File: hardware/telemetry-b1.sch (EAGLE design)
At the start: 119 parts, among them IC1 COPERNICUSSMD, IC10 TPS70933, IC2 TPS70933, IC4 STM32L073CZT6, IC5 TPS62160, IC6 HX1, IC7 LMP7702, IC9 HIH9131, J1 I2C1, J10 TEMP_BAT, J11 DNP, J12 INSOL, J13 SMA_EDGE, J2 I2C2, J3 SMA_EDGE, J4 USD-SOCKET, J5 BAT, J6 SMA_EDGE, J7 SMA_EDGE, J8 TEMP_GPS, J9 TEMP_HOT, K1 ARE104H, K2 ARE104H, Q1 AO3400A, Q2 AO3400A, U1 LTC3105, U2 INA219, Y1 32768, Y2 8M

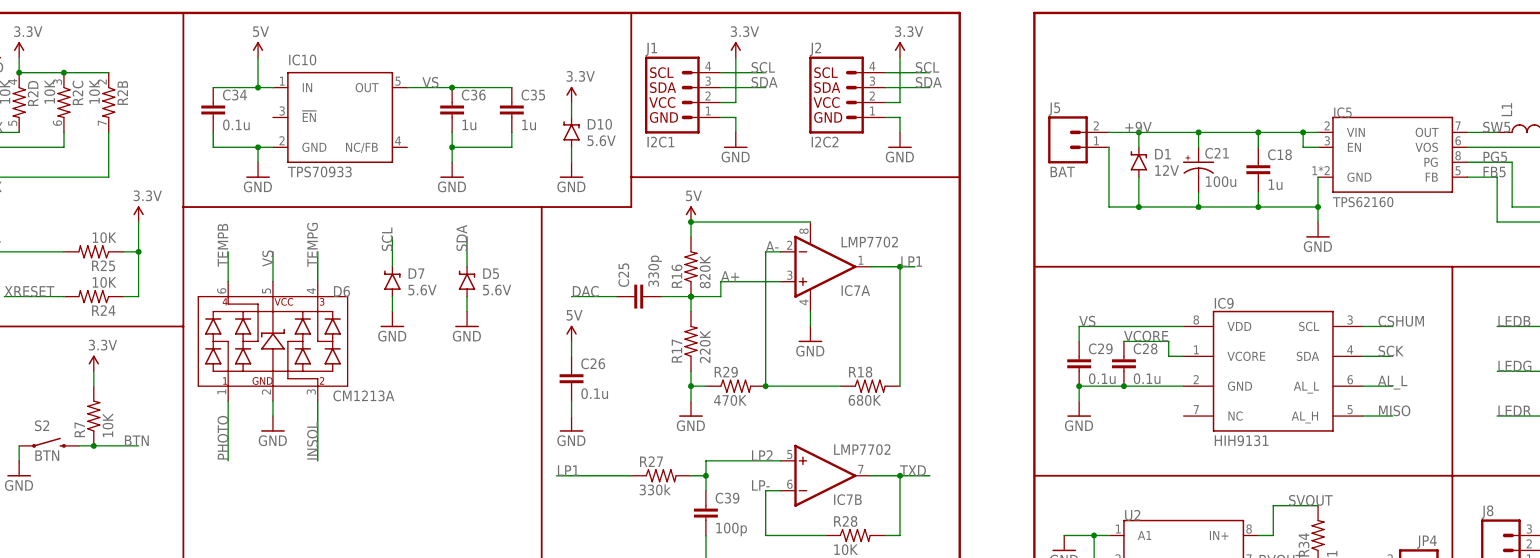
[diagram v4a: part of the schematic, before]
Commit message: Work on layout on beta PCB. Need to swap i2c and swd headers
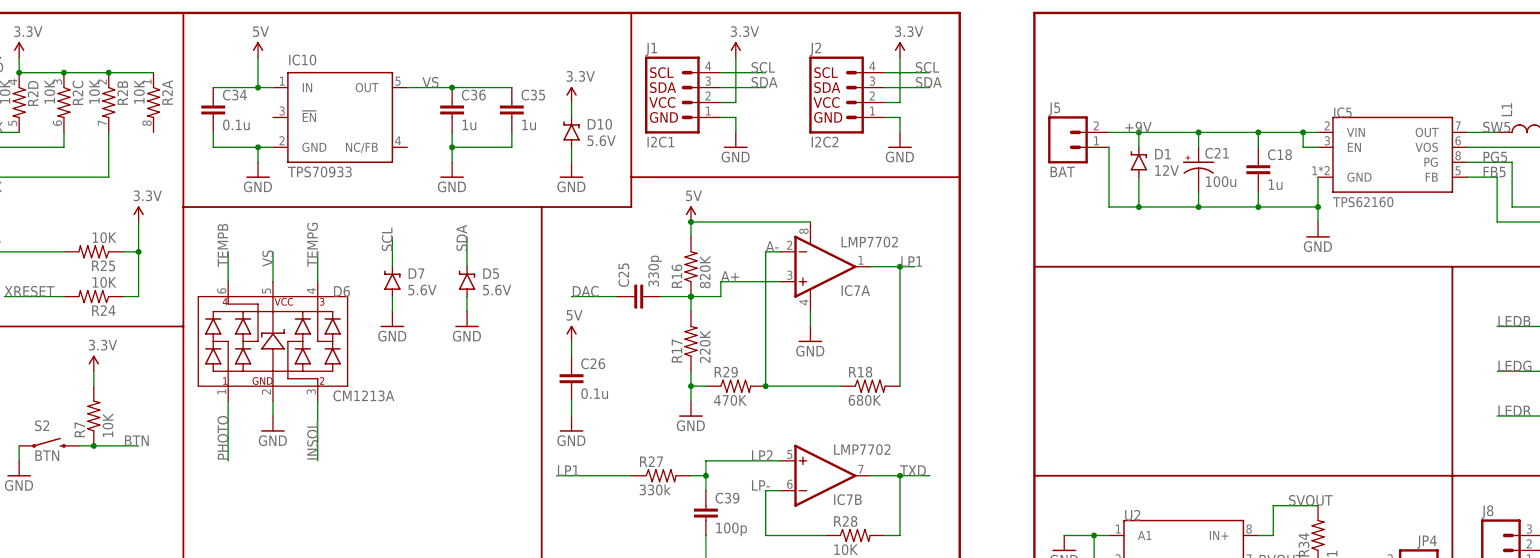
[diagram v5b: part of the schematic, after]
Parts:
- removed C28, C29: 0.1u, SparkFun-Passives:CAP0805
- removed IC9: HIH9131, SparkFun-AnalogIC:HIH6131
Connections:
- removed net AL_L: IC9.AL_L
- removed net VCORE: C28.1, IC9.VCORE
- net 3.3V: now also R2A.1
- net CSHUM: no longer IC9.SCL
- net GND: no longer C28.2, C29.2, IC9.GND
- net MISO: no longer IC9.AL_H
- net SCK: no longer IC9.SDA
- net VS: no longer C29.1, IC9.VDD
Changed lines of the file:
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@@
 <part name="SUPPLY24" library="SparkFun-Aesthetics" deviceset="3.3V" device=""/>
 <part name="C27" library="SparkFun-Passives" deviceset="CAP" device="0805" value="0.1u"/>
-<part name="IC9" library="SparkFun-AnalogIC" deviceset="HIH6131" device="" value="HIH9131"/>
-<part name="C28" library="SparkFun-Passives" deviceset="CAP" device="0805" value="0.1u"/>
-<part name="C29" library="SparkFun-Passives" deviceset="CAP" device="0805" value="0.1u"/>
-<part name="GND29" library="SparkFun-Aesthetics" deviceset="GND" device=""/>
 <part name="J6" library="SparkFun-Connectors" deviceset="SMA_EDGE" device=""/>
 <part name="J7" library="SparkFun-Connectors" deviceset="SMA_EDGE" device=""/>
@@
 <instance part="SUPPLY24" gate="G$1" x="220.98" y="76.2"/>
 <instance part="C27" gate="G$1" x="203.2" y="63.5"/>
-<instance part="IC9" gate="G$1" x="302.26" y="124.46"/>
-<instance part="C28" gate="G$1" x="276.86" y="124.46"/>
-<instance part="C29" gate="G$1" x="269.24" y="124.46"/>
-<instance part="GND29" gate="1" x="269.24" y="116.84"/>
 <instance part="J6" gate="1" x="474.98" y="170.18"/>
 <instance part="J7" gate="1" x="7.62" y="180.34"/>
@@
 <instance part="R34" gate="G$1" x="309.88" y="96.52" rot="R90"/>
 <instance part="JP4" gate="G$1" x="327.66" y="88.9" rot="MR0"/>
+<instance part="R2" gate="A" x="111.76" y="170.18" rot="R270"/>
 </instances>
 <busses>
@@
 <wire x1="203.2" y1="58.42" x2="203.2" y2="60.96" width="0.1524" layer="91"/>
 <junction x="220.98" y="58.42"/>
-</segment>
-<segment>
-<pinref part="GND29" gate="1" pin="GND"/>
-<pinref part="C29" gate="G$1" pin="2"/>
-<wire x1="269.24" y1="119.38" x2="269.24" y2="121.92" width="0.1524" layer="91"/>
-<pinref part="C28" gate="G$1" pin="2"/>
-<wire x1="269.24" y1="121.92" x2="276.86" y2="121.92" width="0.1524" layer="91"/>
-<junction x="269.24" y="121.92"/>
-<pinref part="IC9" gate="G$1" pin="GND"/>
-<wire x1="276.86" y1="121.92" x2="287.02" y2="121.92" width="0.1524" layer="91"/>
-<junction x="276.86" y="121.92"/>
 </segment>
 <segment>
@@
 <wire x1="96.52" y1="175.26" x2="104.14" y2="175.26" width="0.1524" layer="91"/>
 <junction x="96.52" y="175.26"/>
+<pinref part="R2" gate="A" pin="1"/>
+<wire x1="104.14" y1="175.26" x2="111.76" y2="175.26" width="0.1524" layer="91"/>
+<junction x="104.14" y="175.26"/>
 </segment>
 <segment>
@@
 <label x="213.36" y="60.96" size="1.778" layer="95"/>
 </segment>
-<segment>
-<pinref part="IC9" gate="G$1" pin="AL_H"/>
-<wire x1="322.58" y1="116.84" x2="317.5" y2="116.84" width="0.1524" layer="91"/>
-<label x="320.04" y="116.84" size="1.778" layer="95"/>
-</segment>
 </net>
 <net name="SCK" class="0">
@@
 <wire x1="213.36" y1="66.04" x2="223.52" y2="66.04" width="0.1524" layer="91"/>
 <label x="213.36" y="66.04" size="1.778" layer="95"/>
-</segment>
-<segment>
-<pinref part="IC9" gate="G$1" pin="SDA"/>
-<wire x1="322.58" y1="127" x2="317.5" y2="127" width="0.1524" layer="91"/>
-<label x="320.04" y="127" size="1.778" layer="95"/>
 </segment>
 </net>
@@
 </net>
 <net name="CSHUM" class="0">
-<segment>
-<pinref part="IC9" gate="G$1" pin="SCL"/>
-<wire x1="322.58" y1="132.08" x2="317.5" y2="132.08" width="0.1524" layer="91"/>
-<label x="320.04" y="132.08" size="1.778" layer="95"/>
-</segment>
 <segment>
 <pinref part="IC4" gate="G$1" pin="PB13"/>
@@
 </segment>
 </net>
-<net name="VCORE" class="0">
-<segment>
-<pinref part="IC9" gate="G$1" pin="VCORE"/>
-<wire x1="287.02" y1="127" x2="284.48" y2="127" width="0.1524" layer="91"/>
-<wire x1="284.48" y1="127" x2="284.48" y2="129.54" width="0.1524" layer="91"/>
-<pinref part="C28" gate="G$1" pin="1"/>
-<wire x1="284.48" y1="129.54" x2="276.86" y2="129.54" width="0.1524" layer="91"/>
-<label x="276.86" y="129.54" size="1.778" layer="95"/>
-</segment>
-</net>
 <net name="RF_GPS" class="0">
 <segment>
@@
 <wire x1="469.9" y1="109.22" x2="474.98" y2="109.22" width="0.1524" layer="91"/>
 <label x="472.44" y="109.22" size="1.778" layer="95"/>
-</segment>
-</net>
-<net name="AL_L" class="0">
-<segment>
-<pinref part="IC9" gate="G$1" pin="AL_L"/>
-<wire x1="322.58" y1="121.92" x2="317.5" y2="121.92" width="0.1524" layer="91"/>
-<label x="320.04" y="121.92" size="1.778" layer="95"/>
 </segment>
 </net>
@@
 </segment>
 <segment>
-<pinref part="IC9" gate="G$1" pin="VDD"/>
-<pinref part="C29" gate="G$1" pin="1"/>
-<wire x1="287.02" y1="132.08" x2="269.24" y2="132.08" width="0.1524" layer="91"/>
-<wire x1="269.24" y1="132.08" x2="269.24" y2="129.54" width="0.1524" layer="91"/>
-<label x="269.24" y="132.08" size="1.778" layer="95"/>
-</segment>
-<segment>

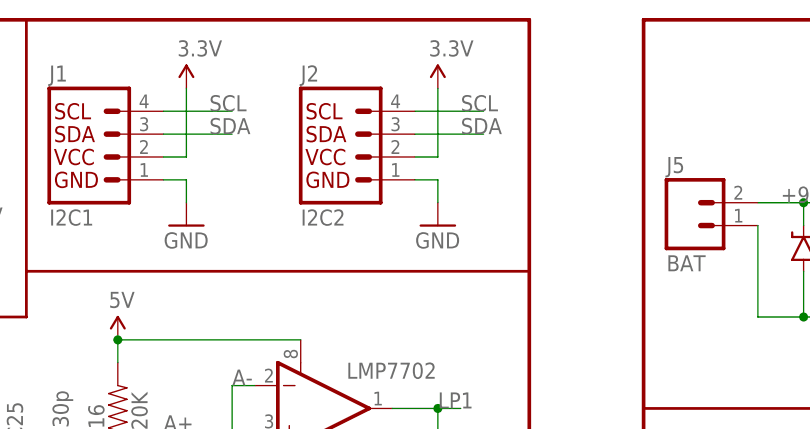
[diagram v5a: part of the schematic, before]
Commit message: Finish routing all traces on beta board. Needs a silkscreen pass.
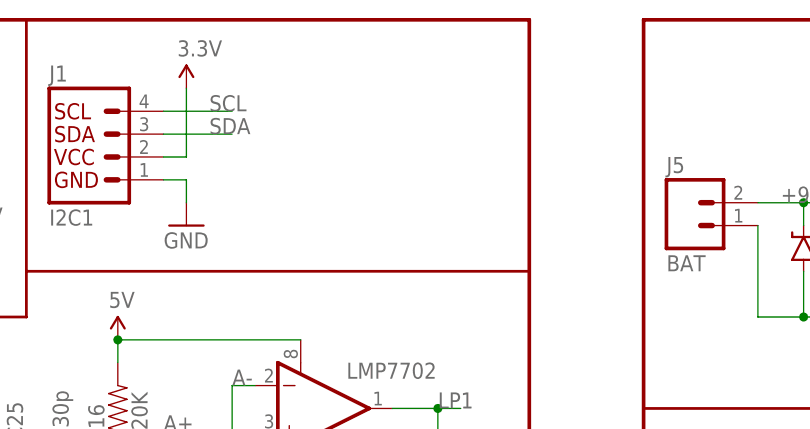
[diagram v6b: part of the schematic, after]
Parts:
- removed J2: I2C2, SparkFun-Connectors:I2C_STANDARD_NO_SILK
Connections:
- net 3.3V: no longer J2.2
- net GND: no longer J2.1
- net SCL: no longer J2.4
- net SDA: no longer J2.3
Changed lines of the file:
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@@
 <part name="SUPPLY12" library="SparkFun-Aesthetics" deviceset="3.3V" device=""/>
 <part name="J1" library="SparkFun-Connectors" deviceset="I2C_STANDARD" device="_NO_SILK" value="I2C1"/>
-<part name="J2" library="SparkFun-Connectors" deviceset="I2C_STANDARD" device="_NO_SILK" value="I2C2"/>
 <part name="SUPPLY13" library="SparkFun-Aesthetics" deviceset="3.3V" device=""/>
-<part name="SUPPLY14" library="SparkFun-Aesthetics" deviceset="3.3V" device=""/>
 <part name="GND17" library="SparkFun-Aesthetics" deviceset="GND" device=""/>
-<part name="GND18" library="SparkFun-Aesthetics" deviceset="GND" device=""/>
 <part name="R2" library="SparkFun-Passives" deviceset="RESISTOR-ARRAY" device="0603-ARV" value="10K"/>
 <part name="IC5" library="HAB" deviceset="TPS62160" device=""/>
@@
 <instance part="SUPPLY12" gate="G$1" x="101.6" y="124.46"/>
 <instance part="J1" gate="G$1" x="198.12" y="165.1"/>
-<instance part="J2" gate="G$1" x="226.06" y="165.1"/>
 <instance part="SUPPLY13" gate="G$1" x="210.82" y="177.8"/>
-<instance part="SUPPLY14" gate="G$1" x="238.76" y="177.8"/>
 <instance part="GND17" gate="1" x="210.82" y="162.56"/>
-<instance part="GND18" gate="1" x="238.76" y="162.56"/>
 <instance part="R2" gate="B" x="104.14" y="170.18" rot="R270"/>
 <instance part="R2" gate="C" x="96.52" y="170.18" rot="R270"/>
@@
 </segment>
 <segment>
-<pinref part="GND18" gate="1" pin="GND"/>
-<wire x1="238.76" y1="165.1" x2="238.76" y2="167.64" width="0.1524" layer="91"/>
-<pinref part="J2" gate="G$1" pin="1"/>
-<wire x1="238.76" y1="167.64" x2="236.22" y2="167.64" width="0.1524" layer="91"/>
-</segment>
-<segment>
 <pinref part="GND17" gate="1" pin="GND"/>
 <wire x1="210.82" y1="165.1" x2="210.82" y2="167.64" width="0.1524" layer="91"/>
@@
 </segment>
 <segment>
-<pinref part="SUPPLY14" gate="G$1" pin="3.3V"/>
-<wire x1="238.76" y1="177.8" x2="238.76" y2="170.18" width="0.1524" layer="91"/>
-<pinref part="J2" gate="G$1" pin="2"/>
-<wire x1="238.76" y1="170.18" x2="236.22" y2="170.18" width="0.1524" layer="91"/>
-</segment>
-<segment>
 <pinref part="J4" gate="G$1" pin="VCC"/>
 <wire x1="223.52" y1="68.58" x2="220.98" y2="68.58" width="0.1524" layer="91"/>
@@
 </segment>
 <segment>
-<pinref part="J2" gate="G$1" pin="4"/>
-<wire x1="243.84" y1="175.26" x2="236.22" y2="175.26" width="0.1524" layer="91"/>
-<label x="241.3" y="175.26" size="1.778" layer="95"/>
-</segment>
-<segment>
 <pinref part="D7" gate="G$1" pin="C"/>
 <wire x1="152.4" y1="142.24" x2="152.4" y2="147.32" width="0.1524" layer="91"/>
@@
 </segment>
 <segment>
-<pinref part="J2" gate="G$1" pin="3"/>
-<wire x1="243.84" y1="172.72" x2="236.22" y2="172.72" width="0.1524" layer="91"/>
-<label x="241.3" y="172.72" size="1.778" layer="95"/>
-</segment>
-<segment>

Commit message: Silkscreen gloss on beta board
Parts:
- J1: value I2C1 -> I2C
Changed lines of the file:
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@@
 <part name="GND16" library="SparkFun-Aesthetics" deviceset="GND" device=""/>
 <part name="SUPPLY12" library="SparkFun-Aesthetics" deviceset="3.3V" device=""/>
-<part name="J1" library="SparkFun-Connectors" deviceset="I2C_STANDARD" device="_NO_SILK" value="I2C1"/>
+<part name="J1" library="SparkFun-Connectors" deviceset="I2C_STANDARD" device="_NO_SILK" value="I2C"/>
 <part name="SUPPLY13" library="SparkFun-Aesthetics" deviceset="3.3V" device=""/>
 <part name="GND17" library="SparkFun-Aesthetics" deviceset="GND" device=""/>

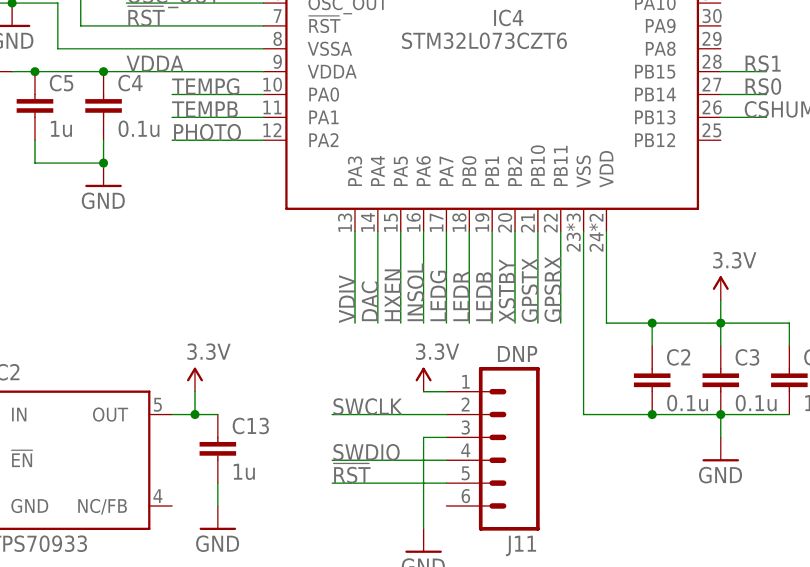
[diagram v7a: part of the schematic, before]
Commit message: Swap HXEN pin to 5VT pin
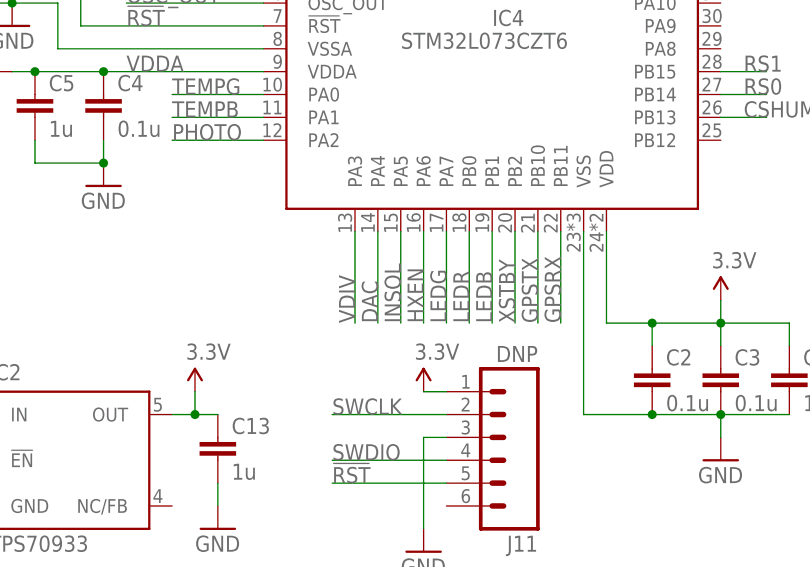
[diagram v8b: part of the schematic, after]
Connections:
- net HXEN: now also IC4.PA6; no longer IC4.PA5
- net INSOL: now also IC4.PA5; no longer IC4.PA6
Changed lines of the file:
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@@
 </segment>
 <segment>
-<pinref part="IC4" gate="G$1" pin="PA5"/>
-<wire x1="60.96" y1="30.48" x2="60.96" y2="40.64" width="0.1524" layer="91"/>
-<label x="60.96" y="30.48" size="1.778" layer="95" rot="R90"/>
+<pinref part="IC4" gate="G$1" pin="PA6"/>
+<wire x1="63.5" y1="30.48" x2="63.5" y2="40.64" width="0.1524" layer="91"/>
+<label x="63.5" y="30.48" size="1.778" layer="95" rot="R90"/>
 </segment>
 </net>
@@
 </segment>
 <segment>
-<pinref part="IC4" gate="G$1" pin="PA6"/>
-<wire x1="63.5" y1="30.48" x2="63.5" y2="40.64" width="0.1524" layer="91"/>
-<label x="63.5" y="30.48" size="1.778" layer="95" rot="R90"/>
-</segment>
-</net>
+<pinref part="IC4" gate="G$1" pin="PA5"/>
+<wire x1="60.96" y1="30.48" x2="60.96" y2="40.64" width="0.1524" layer="91"/>
+<label x="60.96" y="30.48" size="1.778" layer="95" rot="R90"/>
+</segment>
+</net>
